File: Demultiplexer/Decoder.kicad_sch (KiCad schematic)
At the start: 12 parts, among them U401 74HC00, U402 74HC00

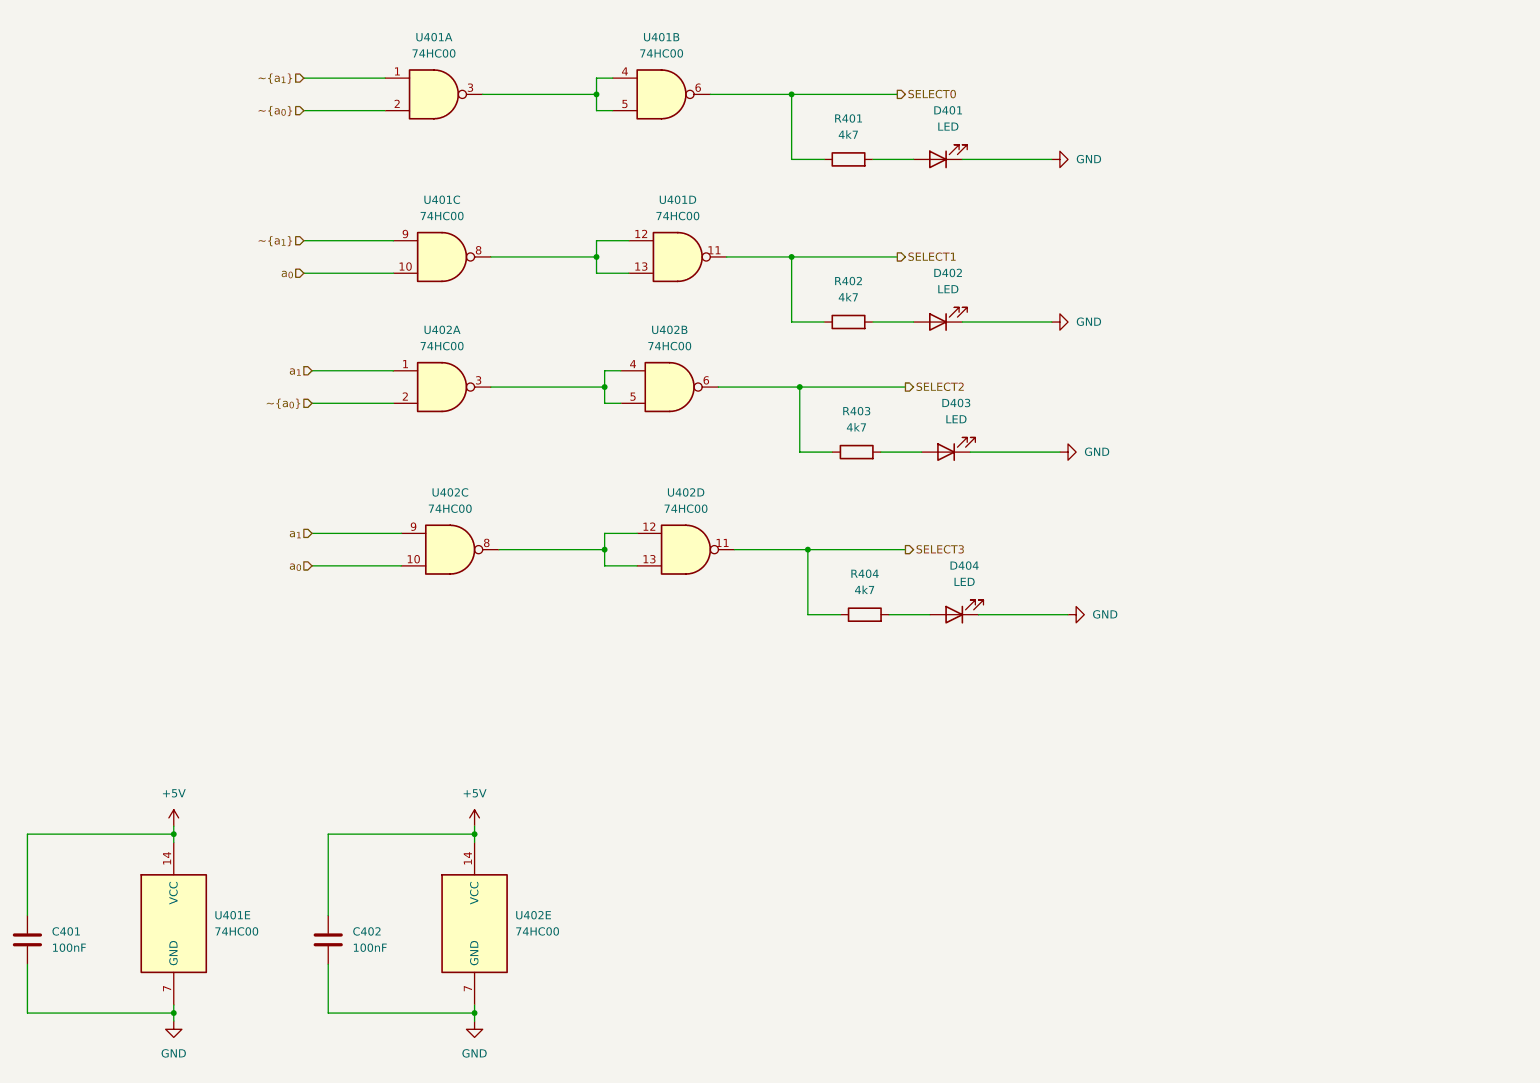
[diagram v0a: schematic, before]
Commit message: Go with individual chips for AND gates
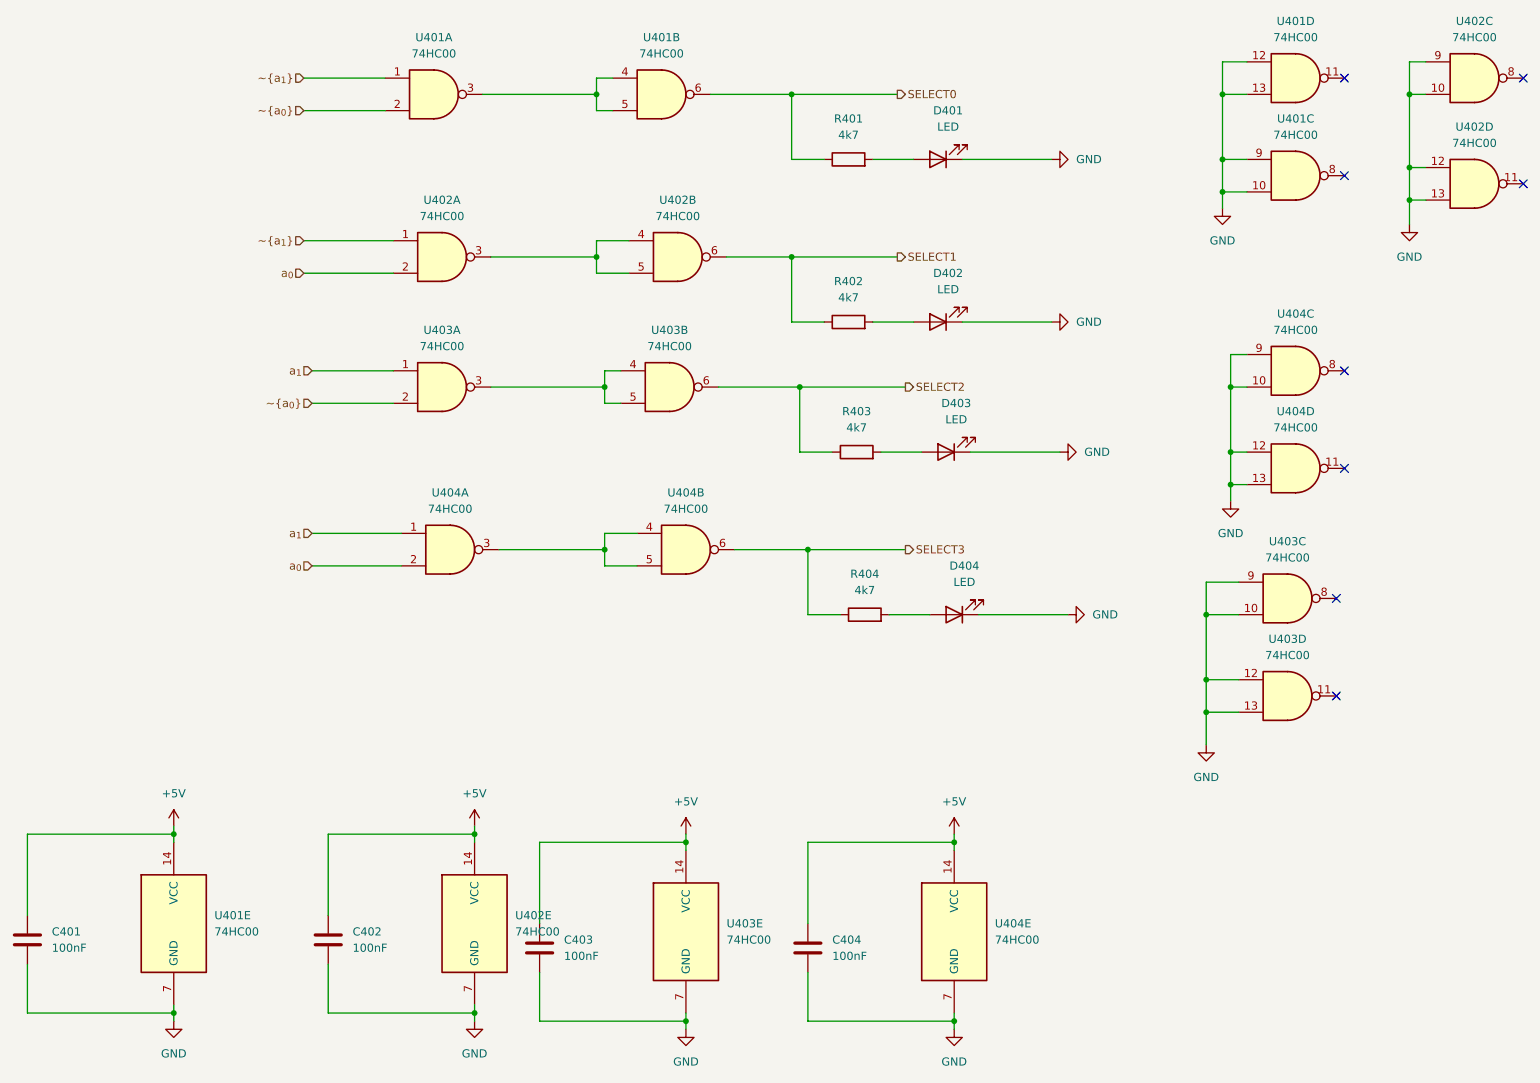
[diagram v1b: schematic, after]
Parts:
- added C403, C404: 100nF, Capacitor_THT:C_Disc_D5.0mm_W2.5mm_P5.00mm, symbol Device:C
- added U403, U404: 74HC00, Package_DIP:DIP-14_W7.62mm_Socket, symbol 74xx:74HC00
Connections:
- net +5V: now also C403.2, C404.2, U403.14 (VCC), U404.14 (VCC)
- net GND: now also U401.10, U401.12, U401.13, U401.9, U402.10, U402.12, U402.13, U402.9, C403.1, C404.1, U403.10, U403.12, U403.13, U403.7 (GND), U403.9, U404.10, U404.12, U404.13, U404.7 (GND), U404.9
- net SELECT1: now also U402.6; no longer U401.11
- net SELECT2: now also U403.6; no longer U402.6
- net SELECT3: now also U404.6; no longer U402.11
- net a_{0}: now also U402.2, U404.2; no longer U401.10, U402.10
- net a_{1}: now also U403.1, U404.1; no longer U402.1, U402.9
- net ~{a_{0}}: now also U403.2; no longer U402.2
- net ~{a_{1}}: now also U402.1; no longer U401.9
- new net: U404.3, U404.4, U404.5
- new net: U403.3, U403.4, U403.5
- now unconnected: U401.8, U402.8
- no-connect marks 0 -> 8
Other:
- moved on the sheet: U401C, U401D, U402A, U402B, U402C, U402D

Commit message: Rethinking NOT gates and starting on output
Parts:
- renumbered C401 to C301, C402 to C302, C403 to C303, C404 to C304, D401 to D301, D402 to D302, D403 to D303, D404 to D304, R401 to R301, R402 to R302, R403 to R303, R404 to R304, U401 to U301, U402 to U302, U403 to U303, U404 to U304
